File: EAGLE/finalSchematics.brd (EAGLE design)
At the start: 100 x 80 mm, 11 parts, among them IC1 STM32F103RBT, Q1 8MHz 131-220

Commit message: Update
WIP
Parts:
- removed SD: (no value), pinhead:1X07
- added P1: DM3CS-SF, DM3CS-SF:HRS_DM3CS-SF
- moved MINIMU-9 90.7 mm to (66.0, 10.2), turned to 180 degrees
- moved GPSANA 54.6 mm to (5.08, 17.8)
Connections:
- removed net CD1: SD.7
- removed net DI: SD.2
- removed net DO: SD.6
- removed net SCL_BPM180: BME280.4, IC1.61
- removed net SDA_BPM180: BME280.5, IC1.62
- removed net VCC: SD.3
- removed net VDD: IC1.19, IC1.32, IC1.48, IC1.64, MINIMU-9.1
- removed net VIN: MINIMU-9.2
- new net MISO: IC1.35, P1.7
- new net MOSI: IC1.36, P1.3
- net +3V3: now also MINIMU-9.5, P1.4
- net CS: now also IC1.43, P1.2; no longer SD.1
- net GND: now also P1.6; no longer SD.5
- net MISO_MODEM: no longer IC1.35
- net MOSI_MODEM: no longer IC1.36
- net SCK: now also IC1.34, P1.5; no longer SD.4
- net SCK_MODEM: no longer IC1.34
- net SCL: now also BME280.4, IC1.19, IC1.32, IC1.48, IC1.61, IC1.64, MINIMU-9.1; no longer MINIMU-9.5
- net SDA: now also BME280.5, IC1.62, MINIMU-9.2; no longer MINIMU-9.4
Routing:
- net SCL: track 0.00 -> 77.6 mm, vias 0 -> 5
- net VDD: track 49.1 -> 0.00 mm, vias 4 -> 0
- net SDA_BPM180: track 29.3 -> 0.00 mm, vias 1 -> 0
- net SDA: track 0.00 -> 29.3 mm, vias 0 -> 1
- net SCL_BPM180: track 28.4 -> 0.00 mm, vias 1 -> 0
- net MOSI_MODEM: track 16.4 -> 0.17 mm
- net MISO_MODEM: track 17.6 -> 9.34 mm
- net SCK_MODEM: track 19.6 -> 12.6 mm
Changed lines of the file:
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@@
 <element name="U$1" library="RFM69mod" package="20X16BOARD" value="RFM69" x="34.29" y="29.21" rot="MR90"/>
 <element name="BME280" library="pinhead" package="1X05/90" value="" x="76.2" y="62.23" rot="MR90"/>
-<element name="SD" library="pinhead" package="1X07" value="" x="15.24" y="-38.1"/>
-<element name="GPSANA" library="roundsolutions" package="ANT-NSG4712-6" value="ANT-NSG4712-6" x="-6.35" y="-35.56"/>
-<element name="MINIMU-9" library="pinhead" package="1X05" value="" x="1.27" y="-53.34"/>
+<element name="GPSANA" library="roundsolutions" package="ANT-NSG4712-6" value="ANT-NSG4712-6" x="5.08" y="17.78"/>
+<element name="MINIMU-9" library="pinhead" package="1X05" value="" x="66.04" y="10.16" rot="R180"/>
+<element name="P1" library="DM3CS-SF" package="HRS_DM3CS-SF" value="DM3CS-SF" x="80.01" y="34.29" rot="R270">
+<attribute name="PRICE" value="1.04 USD" x="80.01" y="34.29" size="1.778" layer="27" rot="R270" display="off"/>
+<attribute name="DESCRIPTION" value="Conn Micro SD Card HDR 8 POS 1.1mm Solder RA SMD Embossed T/R 0.5A" x="80.01" y="34.29" size="1.778" layer="27" rot="R270" display="off"/>
+<attribute name="MP" value="DM3CS-SF" x="80.01" y="34.29" size="1.778" layer="27" rot="R270" display="off"/>
+<attribute name="AVAILABILITY" value="Good" x="80.01" y="34.29" size="1.778" layer="27" rot="R270" display="off"/>
+<attribute name="PACKAGE" value="None" x="80.01" y="34.29" size="1.778" layer="27" rot="R270" display="off"/>
+<attribute name="MF" value="Hirose" x="80.01" y="34.29" size="1.778" layer="27" rot="R270" display="off"/>
+</element>
 </elements>
 <signals>
@@
 <signal name="VBAT">
 <contactref element="IC1" pad="1"/>
-</signal>
-<signal name="VDD">
-<contactref element="IC1" pad="32"/>
-<contactref element="IC1" pad="48"/>
-<contactref element="IC1" pad="64"/>
-<contactref element="IC1" pad="19"/>
-<wire x1="43.12" y1="53.94" x2="43.12" y2="53.4" width="0.4064" layer="1"/>
-<wire x1="43.12" y1="53.4" x2="44.45" y2="52.07" width="0.4064" layer="1"/>
-<wire x1="44.45" y1="50.8" x2="44.45" y2="52.07" width="0.4064" layer="16"/>
-<via x="44.45" y="52.07" extent="1-16" drill="0.6"/>
-<wire x1="33.02" y1="50.8" x2="44.45" y2="50.8" width="0.4064" layer="16"/>
-<wire x1="44.45" y1="52.07" x2="46.99" y2="52.07" width="0.4064" layer="16"/>
-<wire x1="46.99" y1="52.07" x2="46.99" y2="64.77" width="0.4064" layer="16"/>
-<wire x1="45.12" y1="63.44" x2="45.66" y2="63.44" width="0.4064" layer="1"/>
-<wire x1="45.66" y1="63.44" x2="46.99" y2="64.77" width="0.4064" layer="1"/>
-<via x="46.99" y="64.77" extent="1-16" drill="0.6"/>
-<wire x1="33.62" y1="62.44" x2="31.96" y2="62.44" width="0.4064" layer="1"/>
-<wire x1="31.96" y1="62.44" x2="31.75" y2="62.23" width="0.4064" layer="1"/>
-<wire x1="31.75" y1="62.23" x2="31.75" y2="59.69" width="0.4064" layer="1"/>
-<via x="31.75" y="59.69" extent="1-16" drill="0.6"/>
-<wire x1="31.75" y1="59.69" x2="31.75" y2="54.61" width="0.4064" layer="16"/>
-<wire x1="31.75" y1="54.61" x2="31.75" y2="52.07" width="0.4064" layer="16"/>
-<wire x1="31.75" y1="52.07" x2="33.02" y2="50.8" width="0.4064" layer="16"/>
-<wire x1="33.62" y1="55.94" x2="33.08" y2="55.94" width="0.4064" layer="1"/>
-<wire x1="33.08" y1="55.94" x2="31.75" y2="54.61" width="0.4064" layer="1"/>
-<via x="31.75" y="54.61" extent="1-16" drill="0.6"/>
-<contactref element="MINIMU-9" pad="1"/>
-<wire x1="-3.81" y1="-53.34" x2="33.02" y2="50.8" width="0" layer="19" extent="16-16"/>
 </signal>
 <signal name="VSS">
@@
 <wire x1="40.32" y1="76.2" x2="52.07" y2="76.2" width="0.4064" layer="1"/>
 <wire x1="52.07" y1="76.2" x2="58.42" y2="69.85" width="0.4064" layer="1"/>
-<contactref element="SD" pad="5"/>
 <contactref element="MINIMU-9" pad="3"/>
-<wire x1="17.78" y1="-38.1" x2="27.29" y2="37.71" width="0" layer="19" extent="1-1"/>
-<wire x1="1.27" y1="-53.34" x2="17.78" y2="-38.1" width="0" layer="19" extent="1-1"/>
+<contactref element="P1" pad="6"/>
+<wire x1="66.04" y1="10.16" x2="73.81" y2="36.59" width="0" layer="19" extent="1-1"/>
+<wire x1="27.29" y1="37.71" x2="66.04" y2="10.16" width="0" layer="19" extent="1-1"/>
 </signal>
 <signal name="NC">
@@
 </signal>
 <signal name="SCK_MODEM">
-<contactref element="IC1" pad="34"/>
 <contactref element="U$1" pad="SCK"/>
 <wire x1="33.29" y1="37.71" x2="33.02" y2="37.71" width="0.4064" layer="1"/>
 <wire x1="33.02" y1="37.71" x2="33.02" y2="46.99" width="0.4064" layer="1"/>
 <wire x1="33.02" y1="46.99" x2="36.12" y2="46.99" width="0.4064" layer="1"/>
-<wire x1="36.12" y1="46.99" x2="36.12" y2="53.94" width="0.4064" layer="1"/>
 </signal>
 <signal name="MISO_MODEM">
-<contactref element="IC1" pad="35"/>
 <contactref element="U$1" pad="MISO"/>
 <wire x1="35.29" y1="37.71" x2="35.56" y2="37.71" width="0.4064" layer="1"/>
 <wire x1="35.56" y1="37.71" x2="35.56" y2="45.72" width="0.4064" layer="1"/>
 <wire x1="35.56" y1="45.72" x2="36.62" y2="45.72" width="0.4064" layer="1"/>
-<wire x1="36.62" y1="45.72" x2="36.62" y2="53.94" width="0.4064" layer="1"/>
 </signal>
 <signal name="MOSI_MODEM">
-<contactref element="IC1" pad="36"/>
 <contactref element="U$1" pad="MOSI"/>
 <wire x1="37.29" y1="37.71" x2="37.12" y2="37.71" width="0.4064" layer="1"/>
-<wire x1="37.12" y1="37.71" x2="37.12" y2="53.94" width="0.4064" layer="1"/>
 </signal>
 <signal name="N$3">
@@
 <wire x1="26.67" y1="19.05" x2="26.67" y2="19.59" width="0.4064" layer="16"/>
 <wire x1="26.67" y1="19.59" x2="27.29" y2="20.21" width="0.4064" layer="16"/>
-</signal>
-<signal name="SCL_BPM180">
+<contactref element="P1" pad="4"/>
+<contactref element="MINIMU-9" pad="5"/>
+<wire x1="60.96" y1="10.16" x2="73.81" y2="34.39" width="0" layer="19" extent="1-1"/>
+<wire x1="33.02" y1="13.97" x2="60.96" y2="10.16" width="0" layer="19" extent="16-16"/>
+</signal>
+<signal name="SCL">
+<contactref element="IC1" pad="32"/>
+<contactref element="IC1" pad="48"/>
+<contactref element="IC1" pad="64"/>
+<contactref element="IC1" pad="19"/>
+<wire x1="43.12" y1="53.94" x2="43.12" y2="53.4" width="0.4064" layer="1"/>
+<wire x1="43.12" y1="53.4" x2="44.45" y2="52.07" width="0.4064" layer="1"/>
+<wire x1="44.45" y1="50.8" x2="44.45" y2="52.07" width="0.4064" layer="16"/>
+<via x="44.45" y="52.07" extent="1-16" drill="0.6"/>
+<wire x1="33.02" y1="50.8" x2="44.45" y2="50.8" width="0.4064" layer="16"/>
+<wire x1="44.45" y1="52.07" x2="46.99" y2="52.07" width="0.4064" layer="16"/>
+<wire x1="46.99" y1="52.07" x2="46.99" y2="64.77" width="0.4064" layer="16"/>
+<wire x1="45.12" y1="63.44" x2="45.66" y2="63.44" width="0.4064" layer="1"/>
+<wire x1="45.66" y1="63.44" x2="46.99" y2="64.77" width="0.4064" layer="1"/>
+<via x="46.99" y="64.77" extent="1-16" drill="0.6"/>
+<wire x1="33.62" y1="62.44" x2="31.96" y2="62.44" width="0.4064" layer="1"/>
+<wire x1="31.96" y1="62.44" x2="31.75" y2="62.23" width="0.4064" layer="1"/>
+<wire x1="31.75" y1="62.23" x2="31.75" y2="59.69" width="0.4064" layer="1"/>
+<via x="31.75" y="59.69" extent="1-16" drill="0.6"/>
+<wire x1="31.75" y1="59.69" x2="31.75" y2="54.61" width="0.4064" layer="16"/>
+<wire x1="31.75" y1="54.61" x2="31.75" y2="52.07" width="0.4064" layer="16"/>
+<wire x1="31.75" y1="52.07" x2="33.02" y2="50.8" width="0.4064" layer="16"/>
+<wire x1="33.62" y1="55.94" x2="33.08" y2="55.94" width="0.4064" layer="1"/>
+<wire x1="33.08" y1="55.94" x2="31.75" y2="54.61" width="0.4064" layer="1"/>
+<via x="31.75" y="54.61" extent="1-16" drill="0.6"/>
+<contactref element="MINIMU-9" pad="1"/>
 <contactref element="IC1" pad="61"/>
 <contactref element="BME280" pad="4"/>
@@
 <wire x1="62.23" y1="63.5" x2="63.5" y2="64.77" width="0.4064" layer="16"/>
 <wire x1="63.5" y1="64.77" x2="72.39" y2="64.77" width="0.4064" layer="16"/>
-</signal>
-<signal name="SDA_BPM180">
+<wire x1="45.12" y1="63.44" x2="45.12" y2="61.94" width="0" layer="19" extent="1-1"/>
+<wire x1="71.12" y1="10.16" x2="33.02" y2="50.8" width="0" layer="19" extent="16-16"/>
+</signal>
+<signal name="SDA">
+<contactref element="MINIMU-9" pad="2"/>
 <contactref element="IC1" pad="62"/>
 <contactref element="BME280" pad="5"/>
@@
 <wire x1="49.53" y1="63.5" x2="53.34" y2="67.31" width="0.4064" layer="16"/>
 <wire x1="53.34" y1="67.31" x2="72.39" y2="67.31" width="0.4064" layer="16"/>
-</signal>
-<signal name="VCC">
-<contactref element="SD" pad="3"/>
+<wire x1="68.58" y1="10.16" x2="45.12" y2="62.44" width="0" layer="19" extent="1-1"/>
+</signal>
+<signal name="MOSI">
+<contactref element="P1" pad="3"/>
+<contactref element="IC1" pad="36"/>
+<wire x1="73.81" y1="33.29" x2="37.12" y2="53.94" width="0" layer="19" extent="1-1"/>
+</signal>
+<signal name="SCK">
+<contactref element="P1" pad="5"/>
+<contactref element="IC1" pad="34"/>
+<wire x1="73.81" y1="35.49" x2="36.12" y2="53.94" width="0" layer="19" extent="1-1"/>
+</signal>
+<signal name="MISO">
+<contactref element="P1" pad="7"/>
+<contactref element="IC1" pad="35"/>
+<wire x1="73.81" y1="37.69" x2="36.62" y2="53.94" width="0" layer="19" extent="1-1"/>
 </signal>
 <signal name="CS">
-<contactref element="SD" pad="1"/>
-</signal>
-<signal name="DI">
-<contactref element="SD" pad="2"/>
-</signal>
-<signal name="SCK">
-<contactref element="SD" pad="4"/>
-</signal>
-<signal name="DO">
-<contactref element="SD" pad="6"/>
-</signal>
-<signal name="CD1">
-<contactref element="SD" pad="7"/>
-</signal>
-<signal name="SCL">
-<contactref element="MINIMU-9" pad="5"/>
-</signal>
-<signal name="SDA">
-<contactref element="MINIMU-9" pad="4"/>
-</signal>
-<signal name="VIN">
-<contactref element="MINIMU-9" pad="2"/>
+<contactref element="P1" pad="2"/>
+<contactref element="IC1" pad="43"/>
+<wire x1="40.62" y1="53.94" x2="73.81" y2="32.19" width="0" layer="19" extent="1-1"/>
 </signal>
 </signals>

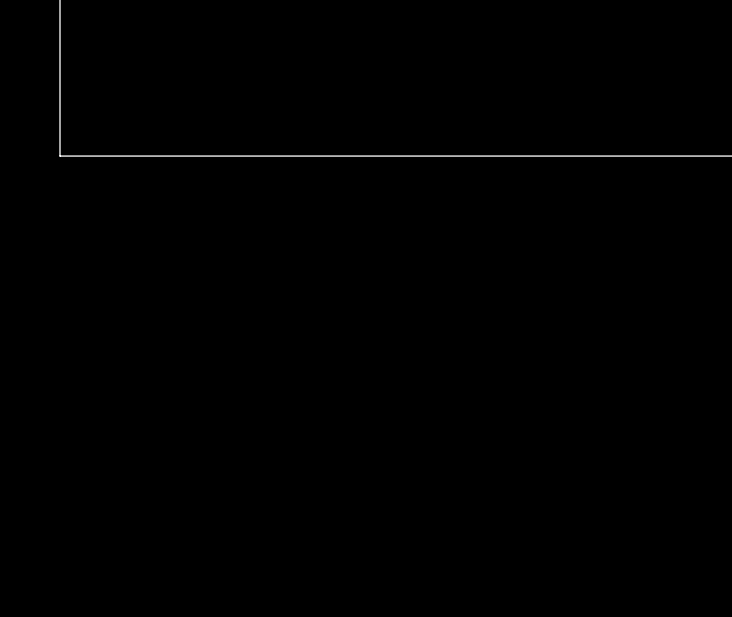
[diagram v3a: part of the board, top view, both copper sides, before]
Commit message: Add GPS components
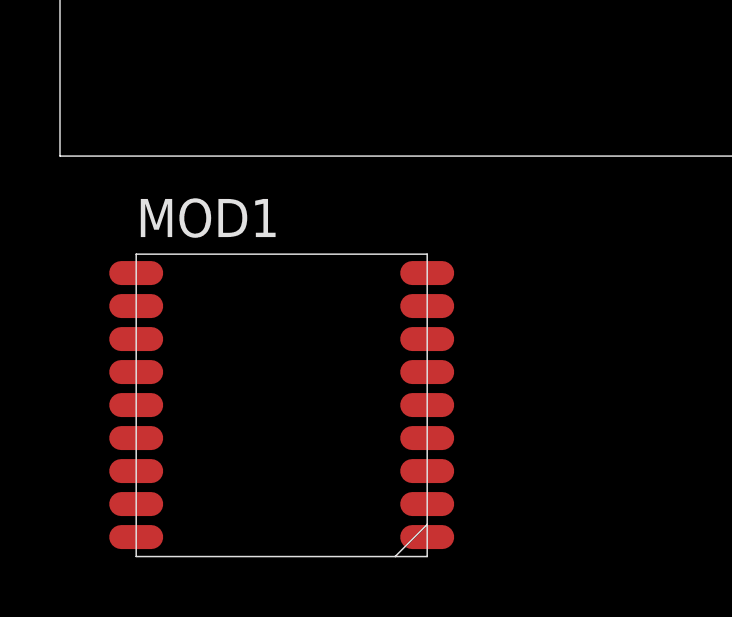
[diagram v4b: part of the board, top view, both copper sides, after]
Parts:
- added MOD1: (no value), components:L70B-GPS
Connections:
- new net VCC: MOD1.VCC
- net GND: now also MOD1.GND1, MOD1.GND2, MOD1.GND3
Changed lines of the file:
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@@
 <?xml version="1.0" encoding="utf-8"?>
 <!DOCTYPE eagle SYSTEM "eagle.dtd">
-<eagle version="8.0.0">
+<eagle version="8.0.1">
 <drawing>
 <settings>
@@
 <attribute name="MF" value="Hirose" x="80.01" y="34.29" size="1.778" layer="27" rot="R270" display="off"/>
 </element>
+<element name="MOD1" library="components" package="L70B-GPS" value="" x="2.54" y="-12.7"/>
 </elements>
 <signals>
@@
 <contactref element="MINIMU-9" pad="3"/>
 <contactref element="P1" pad="6"/>
+<contactref element="MOD1" pad="GND1"/>
+<contactref element="MOD1" pad="GND2"/>
+<contactref element="MOD1" pad="GND3"/>
+<wire x1="52.07" y1="49.53" x2="73.81" y2="36.59" width="0" layer="19" extent="1-1"/>
 <wire x1="66.04" y1="10.16" x2="73.81" y2="36.59" width="0" layer="19" extent="1-1"/>
-<wire x1="27.29" y1="37.71" x2="66.04" y2="10.16" width="0" layer="19" extent="1-1"/>
+<wire x1="2.54" y1="-3.9" x2="27.29" y2="37.71" width="0" layer="19" extent="1-1"/>
+<wire x1="2.54" y1="-6.1" x2="2.54" y2="-3.9" width="0" layer="19" extent="1-1"/>
+<wire x1="12.24" y1="-12.7" x2="2.54" y2="-6.1" width="0" layer="19" extent="1-1"/>
 </signal>
 <signal name="NC">
@@
 <wire x1="40.62" y1="53.94" x2="73.81" y2="32.19" width="0" layer="19" extent="1-1"/>
 </signal>
+<signal name="VCC">
+<contactref element="MOD1" pad="VCC"/>
+</signal>
 </signals>
